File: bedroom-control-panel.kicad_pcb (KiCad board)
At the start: 2 copper layers, 100 x 25 mm, 37 parts, among them IC1 TLV1117-33CDCYG3, J1 USB4105-GF-A, U1 ESP32-S3-WROOM-1-N8R8, U2 PEC11L-4315F-S0009

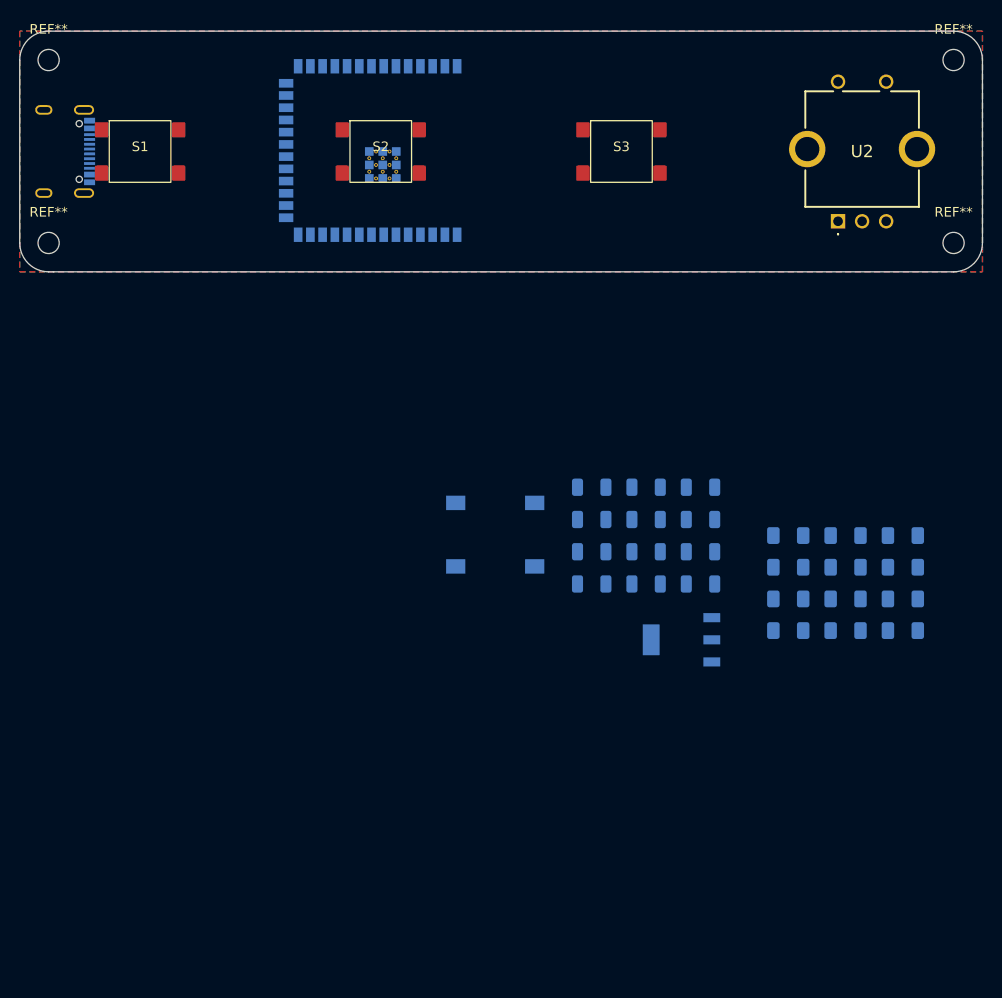
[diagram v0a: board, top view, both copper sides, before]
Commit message: schematic complete, added bme680
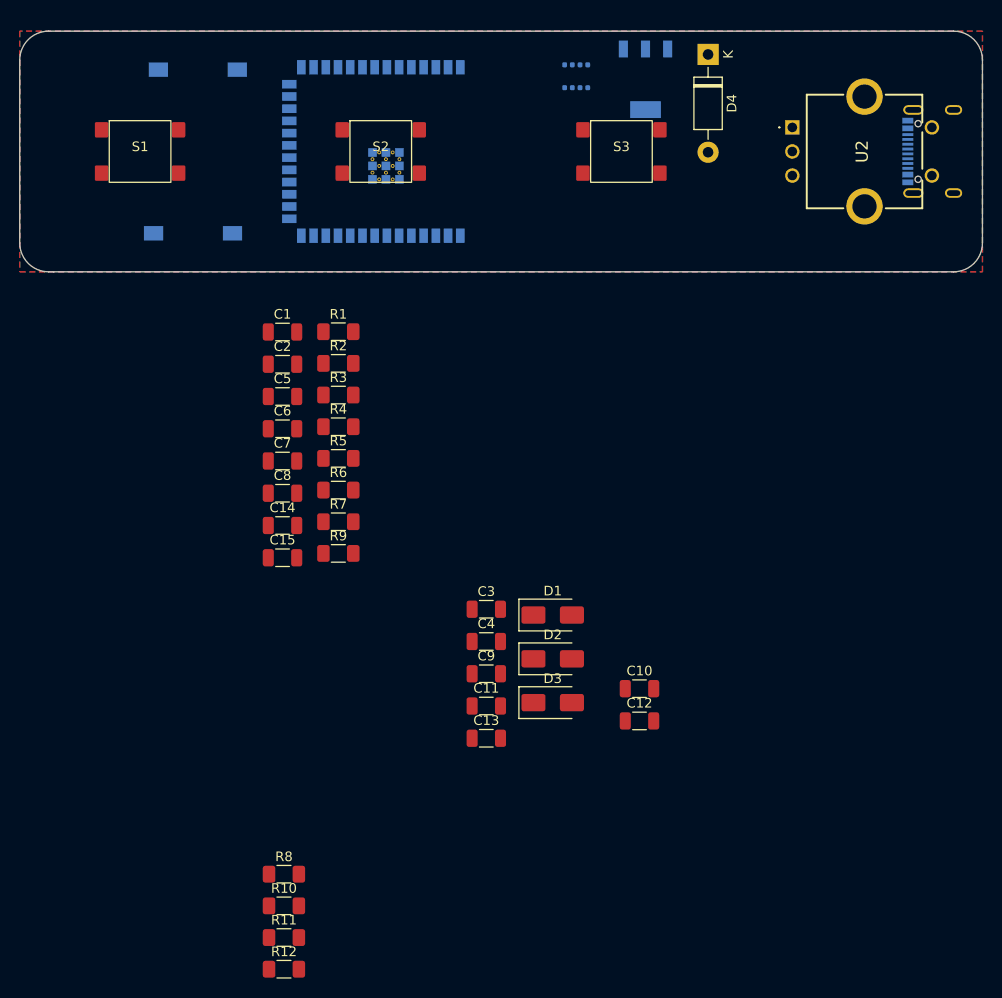
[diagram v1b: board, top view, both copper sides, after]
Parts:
- removed REF** (x4): MountingHole_2.2mm_M2, MountingHole:MountingHole_2.2mm_M2
- added C13: 10uF, Capacitor_SMD:C_1206_3216Metric, F.Cu at (78.5, 103.5)
- added C14: 10uF, Capacitor_SMD:C_1206_3216Metric, F.Cu at (57.3, 81.3)
- added C15: 0.1uF, Capacitor_SMD:C_1206_3216Metric, F.Cu at (57.3, 84.7)
- added D1: SMAJ5.0CA, Diode_SMD:D_SMA, F.Cu at (85.4, 90.7)
- added D2: SMAJ5.0CA, Diode_SMD:D_SMA, F.Cu at (85.4, 95.2)
- added D3: SMAJ5.0CA, Diode_SMD:D_SMA, F.Cu at (85.4, 99.8)
- added D4: 1N5819, Diode_THT:D_DO-41_SOD81_P10.16mm_Horizontal, F.Cu at (101.5, 32.4)
- added U3: BME680, Package_LGA:Bosch_LGA-8_3x3mm_P0.8mm_ClockwisePinNumbering, B.Cu at (87.8, 34.7)
- C1: value 0.1uF -> 0.01uF; moved to F.Cu
- C10: value 1uF -> 100uF; moved to F.Cu
- C11: value 0.01uF -> 1uF; moved to F.Cu
- C12: value 0.01uF -> 100uF; moved to F.Cu
- C2: value 10uF -> 0.01uF; moved to F.Cu
- C3: value 1uF -> 0.1uF; moved to F.Cu
- C4: value 1uF -> 10uF; moved to F.Cu
- C5, C6, C7, R5, R6, R7, R9: moved to F.Cu
- C8, C9: value 100uF -> 1uF; moved to F.Cu
- R1, R2: value 10k -> 10K; moved to F.Cu
- R10, R12: value 10K -> 10k; moved to F.Cu
- R11, R8: value 10K -> 5k1; moved to F.Cu
- R3, R4: value 5K1 -> 10K; moved to F.Cu
- moved J1 94.5 mm to (127.0, 42.5), turned to -90 degrees
- moved R8 63.6 mm to (57.4, 117.6), turned to 0 degrees
- moved R11 63.1 mm to (57.4, 124.2), turned to 0 degrees
- moved R10 63.1 mm to (57.4, 120.9), turned to 0 degrees
- moved R12 63.1 mm to (57.4, 127.4), turned to 0 degrees
- moved R1 62.3 mm to (63.1, 61.2), turned to 0 degrees
- moved R2 62.3 mm to (63.1, 64.5), turned to 0 degrees
- moved R3 62.3 mm to (63.1, 67.8), turned to 0 degrees
- moved R4 62.3 mm to (63.1, 71.1), turned to 0 degrees
- moved S5 60.1 mm to (48.5, 34.0), turned to 0 degrees
- moved IC1 58.3 mm to (95.0, 35.0), turned to -90 degrees
- moved R5 53.3 mm to (63.1, 74.4), turned to 0 degrees
- moved R6 53.3 mm to (63.1, 77.7), turned to 0 degrees
- moved R7 53.3 mm to (63.1, 81.0), turned to 0 degrees
- moved R9 46.8 mm to (63.1, 84.2), turned to 0 degrees
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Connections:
- C1 pad 1: +3V3 -> ENCODER_B
- C10 pad 1: GND -> +5V
- C10 pad 2: Net-(U2-NO) -> GND
- C11 pad 1: ENCODER_B -> GPIO_0
- C12 pad 1: ENCODER_A -> +3V3
- C2 pad 1: +3V3 -> ENCODER_A
- C3 pad 1: ESP_EN -> +3V3
- C4 pad 1: GPIO_0 -> +3V3
- C5 pad 1: Net-(C5-Pad1) -> GND
- C5 pad 2: GND -> Net-(U2-NO)
- C8 pad 1: +3V3 -> Net-(C8-Pad1)
- C9 pad 1: USB_5V -> ESP_EN
- IC1 pad 3: USB_5V -> +5V
- R1 pad 2: ESP_EN -> Net-(U2-CHANNEL_B)
- R10 pad 2: Net-(U2-CHANNEL_B) -> ESP_EN
- R11 pad 1: ENCODER_B -> Net-(J1-CC2)
- R11 pad 2: Net-(U2-CHANNEL_B) -> GND
- R12 pad 1: ENCODER_A -> +3V3
- R12 pad 2: Net-(U2-CHANNEL_A) -> GPIO_0
- R2 pad 1: +3V3 -> ENCODER_B
- R2 pad 2: GPIO_0 -> Net-(U2-CHANNEL_B)
- R3 pad 1: Net-(J1-CC1) -> +3V3
- R3 pad 2: GND -> Net-(U2-CHANNEL_A)
- R4 pad 1: Net-(J1-CC2) -> ENCODER_A
- R4 pad 2: GND -> Net-(U2-CHANNEL_A)
- R5 pad 1: BTN_1 -> Net-(U2-NO)
- R5 pad 2: Net-(C5-Pad1) -> BTN_4
- R6 pad 1: BTN_2 -> BTN_1
- R7 pad 1: BTN_3 -> BTN_2
- R8 pad 1: Net-(U2-NO) -> Net-(J1-CC1)
- R8 pad 2: BTN_4 -> GND
- R9 pad 1: +3V3 -> BTN_3
- R9 pad 2: Net-(U2-CHANNEL_A) -> Net-(C8-Pad1)
- S1 pad 3: Net-(C5-Pad1) -> Net-(C6-Pad1)
- S1 pad 4: Net-(C5-Pad1) -> Net-(C6-Pad1)
- S2 pad 3: Net-(C6-Pad1) -> Net-(C7-Pad1)
- S2 pad 4: Net-(C6-Pad1) -> Net-(C7-Pad1)
- S3 pad 3: Net-(C7-Pad1) -> Net-(C8-Pad1)
- S3 pad 4: Net-(C7-Pad1) -> Net-(C8-Pad1)
- U1 pad 13: unconnected-(U1-IO19-Pad13) -> USB_D-
- U1 pad 14: unconnected-(U1-IO20-Pad14) -> USB_D+
- U1 pad 18: unconnected-(U1-IO10-Pad18) -> SDA
- U1 pad 19: USB_D- -> SCL
- U1 pad 20: USB_D+ -> unconnected-(U1-IO12-Pad20)
